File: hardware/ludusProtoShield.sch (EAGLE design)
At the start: 65 parts, among them U1 ARDUINO, U2 TB6612FNG

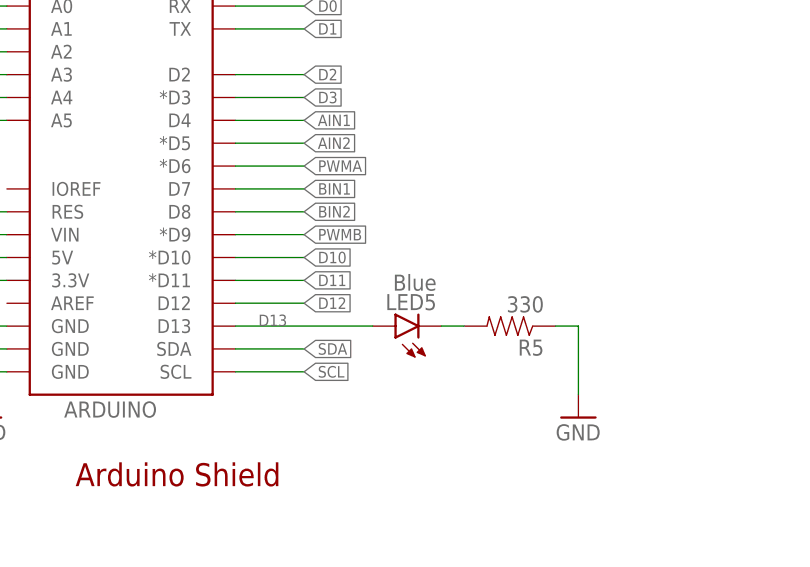
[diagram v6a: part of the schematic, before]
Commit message: Nudged test points and fixed led prod_id for led 5
moved test points to avoid selective solder coverage and updated led 5
to include production id.
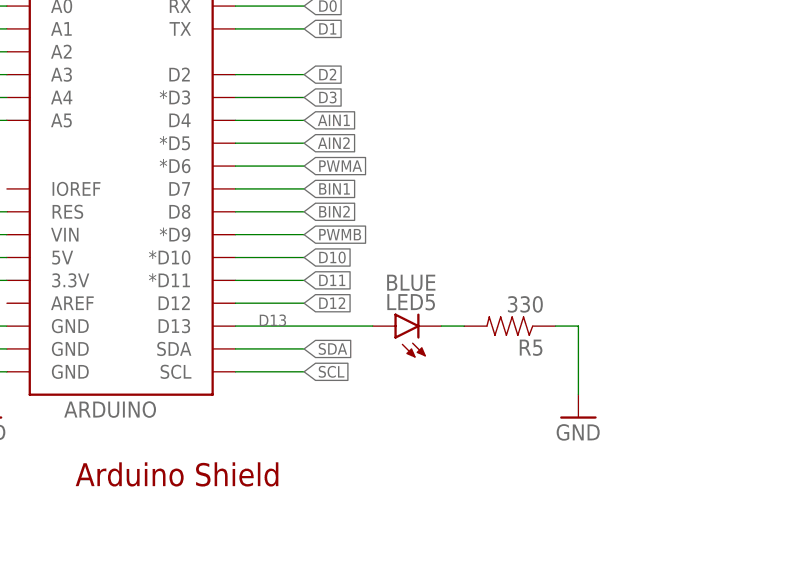
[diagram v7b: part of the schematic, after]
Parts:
- LED5: value Blue -> BLUE; device SparkFun-LED:LED0603 -> SparkFun-LED:LED-BLUE0603
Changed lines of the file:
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@@
 <?xml version="1.0" encoding="utf-8"?>
 <!DOCTYPE eagle SYSTEM "eagle.dtd">
-<eagle version="7.2.0">
+<eagle version="7.1.0">
 <drawing>
 <settings>
@@
 <grid distance="0.1" unitdist="inch" unit="inch" style="lines" multiple="1" display="no" altdistance="0.01" altunitdist="inch" altunit="inch"/>
 <layers>
-<layer number="1" name="Top" color="4" fill="1" visible="yes" active="no"/>
-<layer number="2" name="Route2" color="1" fill="3" visible="yes" active="no"/>
-<layer number="3" name="Route3" color="4" fill="3" visible="yes" active="no"/>
-<layer number="4" name="Route4" color="1" fill="4" visible="yes" active="no"/>
-<layer number="5" name="Route5" color="4" fill="4" visible="yes" active="no"/>
-<layer number="6" name="Route6" color="1" fill="8" visible="yes" active="no"/>
-<layer number="7" name="Route7" color="4" fill="8" visible="yes" active="no"/>
-<layer number="8" name="Route8" color="1" fill="2" visible="yes" active="no"/>
-<layer number="9" name="Route9" color="4" fill="2" visible="yes" active="no"/>
-<layer number="10" name="Route10" color="1" fill="7" visible="yes" active="no"/>
-<layer number="11" name="Route11" color="4" fill="7" visible="yes" active="no"/>
-<layer number="12" name="Route12" color="1" fill="5" visible="yes" active="no"/>
-<layer number="13" name="Route13" color="4" fill="5" visible="yes" active="no"/>
-<layer number="14" name="Route14" color="1" fill="6" visible="yes" active="no"/>
-<layer number="15" name="Route15" color="4" fill="6" visible="yes" active="no"/>
-<layer number="16" name="Bottom" color="1" fill="1" visible="yes" active="no"/>
-<layer number="17" name="Pads" color="2" fill="1" visible="yes" active="no"/>
-<layer number="18" name="Vias" color="2" fill="1" visible="yes" active="no"/>
-<layer number="19" name="Unrouted" color="6" fill="1" visible="yes" active="no"/>
-<layer number="20" name="Dimension" color="15" fill="1" visible="yes" active="no"/>
-<layer number="21" name="tPlace" color="16" fill="1" visible="yes" active="no"/>
-<layer number="22" name="bPlace" color="14" fill="1" visible="yes" active="no"/>
-<layer number="23" name="tOrigins" color="15" fill="1" visible="yes" active="no"/>
-<layer number="24" name="bOrigins" color="15" fill="1" visible="yes" active="no"/>
-<layer number="25" name="tNames" color="7" fill="1" visible="yes" active="no"/>
-<layer number="26" name="bNames" color="7" fill="1" visible="yes" active="no"/>
-<layer number="27" name="tValues" color="7" fill="1" visible="yes" active="no"/>
-<layer number="28" name="bValues" color="7" fill="1" visible="yes" active="no"/>
+<layer number="1" name="Top" color="4" fill="1" visible="no" active="no"/>
+<layer number="2" name="Route2" color="1" fill="3" visible="no" active="no"/>
+<layer number="3" name="Route3" color="4" fill="3" visible="no" active="no"/>
+<layer number="4" name="Route4" color="1" fill="4" visible="no" active="no"/>
+<layer number="5" name="Route5" color="4" fill="4" visible="no" active="no"/>
+<layer number="6" name="Route6" color="1" fill="8" visible="no" active="no"/>
+<layer number="7" name="Route7" color="4" fill="8" visible="no" active="no"/>
+<layer number="8" name="Route8" color="1" fill="2" visible="no" active="no"/>
+<layer number="9" name="Route9" color="4" fill="2" visible="no" active="no"/>
+<layer number="10" name="Route10" color="1" fill="7" visible="no" active="no"/>
+<layer number="11" name="Route11" color="4" fill="7" visible="no" active="no"/>
+<layer number="12" name="Route12" color="1" fill="5" visible="no" active="no"/>
+<layer number="13" name="Route13" color="4" fill="5" visible="no" active="no"/>
+<layer number="14" name="Route14" color="1" fill="6" visible="no" active="no"/>
+<layer number="15" name="Route15" color="4" fill="6" visible="no" active="no"/>
+<layer number="16" name="Bottom" color="1" fill="1" visible="no" active="no"/>
+<layer number="17" name="Pads" color="2" fill="1" visible="no" active="no"/>
+<layer number="18" name="Vias" color="2" fill="1" visible="no" active="no"/>
+<layer number="19" name="Unrouted" color="6" fill="1" visible="no" active="no"/>
+<layer number="20" name="Dimension" color="15" fill="1" visible="no" active="no"/>
+<layer number="21" name="tPlace" color="16" fill="1" visible="no" active="no"/>
+<layer number="22" name="bPlace" color="14" fill="1" visible="no" active="no"/>
+<layer number="23" name="tOrigins" color="15" fill="1" visible="no" active="no"/>
+<layer number="24" name="bOrigins" color="15" fill="1" visible="no" active="no"/>
+<layer number="25" name="tNames" color="7" fill="1" visible="no" active="no"/>
+<layer number="26" name="bNames" color="7" fill="1" visible="no" active="no"/>
+<layer number="27" name="tValues" color="7" fill="1" visible="no" active="no"/>
+<layer number="28" name="bValues" color="7" fill="1" visible="no" active="no"/>
 <layer number="29" name="tStop" color="7" fill="3" visible="no" active="no"/>
 <layer number="30" name="bStop" color="7" fill="6" visible="no" active="no"/>
@@
 <layer number="35" name="tGlue" color="7" fill="4" visible="no" active="no"/>
 <layer number="36" name="bGlue" color="7" fill="5" visible="no" active="no"/>
-<layer number="37" name="tTest" color="7" fill="1" visible="yes" active="no"/>
-<layer number="38" name="bTest" color="7" fill="1" visible="yes" active="no"/>
+<layer number="37" name="tTest" color="7" fill="1" visible="no" active="no"/>
+<layer number="38" name="bTest" color="7" fill="1" visible="no" active="no"/>
 <layer number="39" name="tKeepout" color="4" fill="11" visible="no" active="no"/>
 <layer number="40" name="bKeepout" color="1" fill="11" visible="no" active="no"/>
@@
 <layer number="44" name="Drills" color="7" fill="1" visible="no" active="no"/>
 <layer number="45" name="Holes" color="7" fill="1" visible="no" active="no"/>
-<layer number="46" name="Milling" color="3" fill="1" visible="yes" active="no"/>
-<layer number="47" name="Measures" color="7" fill="1" visible="yes" active="no"/>
-<layer number="48" name="Document" color="7" fill="1" visible="yes" active="no"/>
-<layer number="49" name="Reference" color="7" fill="1" visible="yes" active="no"/>
-<layer number="50" name="dxf" color="7" fill="1" visible="yes" active="no"/>
-<layer number="51" name="tDocu" color="6" fill="1" visible="yes" active="no"/>
-<layer number="52" name="bDocu" color="7" fill="1" visible="yes" active="no"/>
-<layer number="53" name="tGND_GNDA" color="7" fill="9" visible="yes" active="no"/>
-<layer number="54" name="bGND_GNDA" color="1" fill="9" visible="yes" active="no"/>
-<layer number="56" name="wert" color="7" fill="1" visible="yes" active="no"/>
-<layer number="57" name="tCAD" color="7" fill="1" visible="yes" active="no"/>
-<layer number="59" name="tCarbon" color="7" fill="1" visible="yes" active="no"/>
-<layer number="60" name="bCarbon" color="7" fill="1" visible="yes" active="no"/>
+<layer number="46" name="Milling" color="3" fill="1" visible="no" active="no"/>
+<layer number="47" name="Measures" color="7" fill="1" visible="no" active="no"/>
+<layer number="48" name="Document" color="7" fill="1" visible="no" active="no"/>
+<layer number="49" name="Reference" color="7" fill="1" visible="no" active="no"/>
+<layer number="50" name="dxf" color="7" fill="1" visible="no" active="no"/>
+<layer number="51" name="tDocu" color="6" fill="1" visible="no" active="no"/>
+<layer number="52" name="bDocu" color="7" fill="1" visible="no" active="no"/>
+<layer number="53" name="tGND_GNDA" color="7" fill="9" visible="no" active="no"/>
+<layer number="54" name="bGND_GNDA" color="1" fill="9" visible="no" active="no"/>
+<layer number="56" name="wert" color="7" fill="1" visible="no" active="no"/>
+<layer number="57" name="tCAD" color="7" fill="1" visible="no" active="no"/>
+<layer number="59" name="tCarbon" color="7" fill="1" visible="no" active="no"/>
+<layer number="60" name="bCarbon" color="7" fill="1" visible="no" active="no"/>
 <layer number="90" name="Modules" color="5" fill="1" visible="yes" active="yes"/>
 <layer number="91" name="Nets" color="2" fill="1" visible="yes" active="yes"/>
@@
 <part name="JP19" library="SparkFun-Connectors" deviceset="M03" device="LOCK" value="A5"/>
 <part name="GND2" library="SparkFun" deviceset="GND" device=""/>
-<part name="LED5" library="SparkFun-LED" deviceset="LED" device="0603" value="Blue"/>
+<part name="LED5" library="SparkFun-LED" deviceset="LED-BLUE" device="0603" value="BLUE"/>
 <part name="R5" library="SparkFun-Resistors" deviceset="330OHM1/10W1%(0603)" device="" value="330"/>
 <part name="GND6" library="SparkFun" deviceset="GND" device=""/>
